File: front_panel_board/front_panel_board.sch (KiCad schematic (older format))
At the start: 9 parts, among them J1 Molex_SL_01x02_Male, J2 Conn_02x05_Odd_Even, J3 Molex_SL_01x02_Male, SW1 SW_Rotary8, SW2 SW_SPST

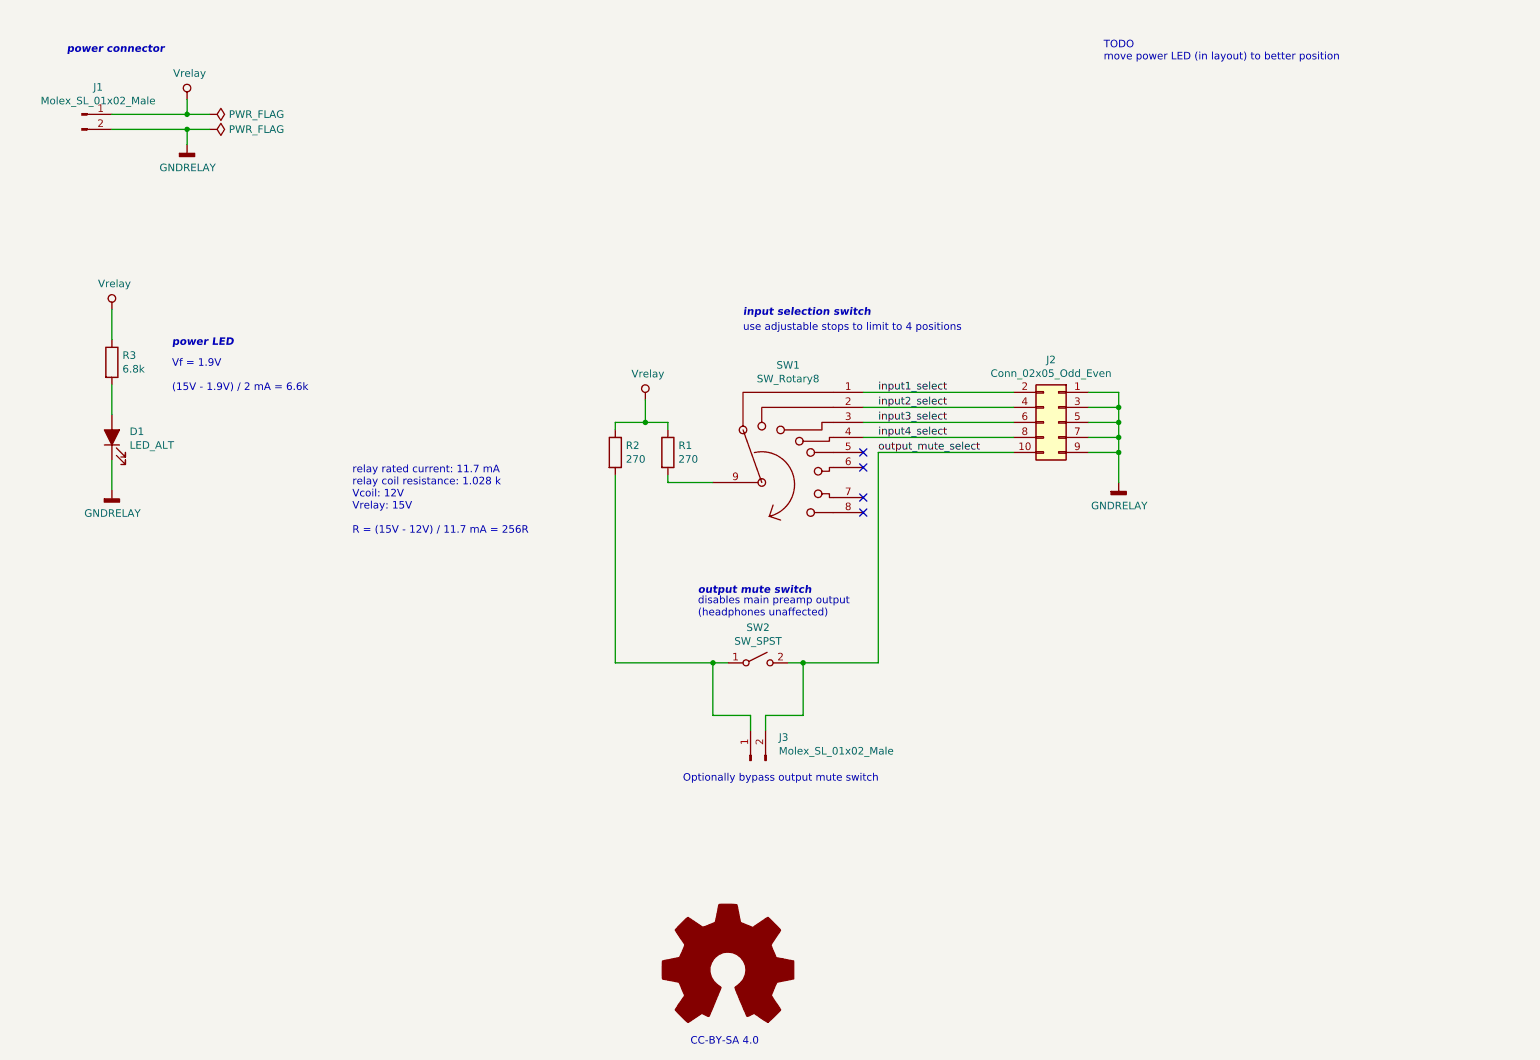
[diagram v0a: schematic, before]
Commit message: update switch symbol/footprint, add second relay control connector, and re-layout (LED not laid out)
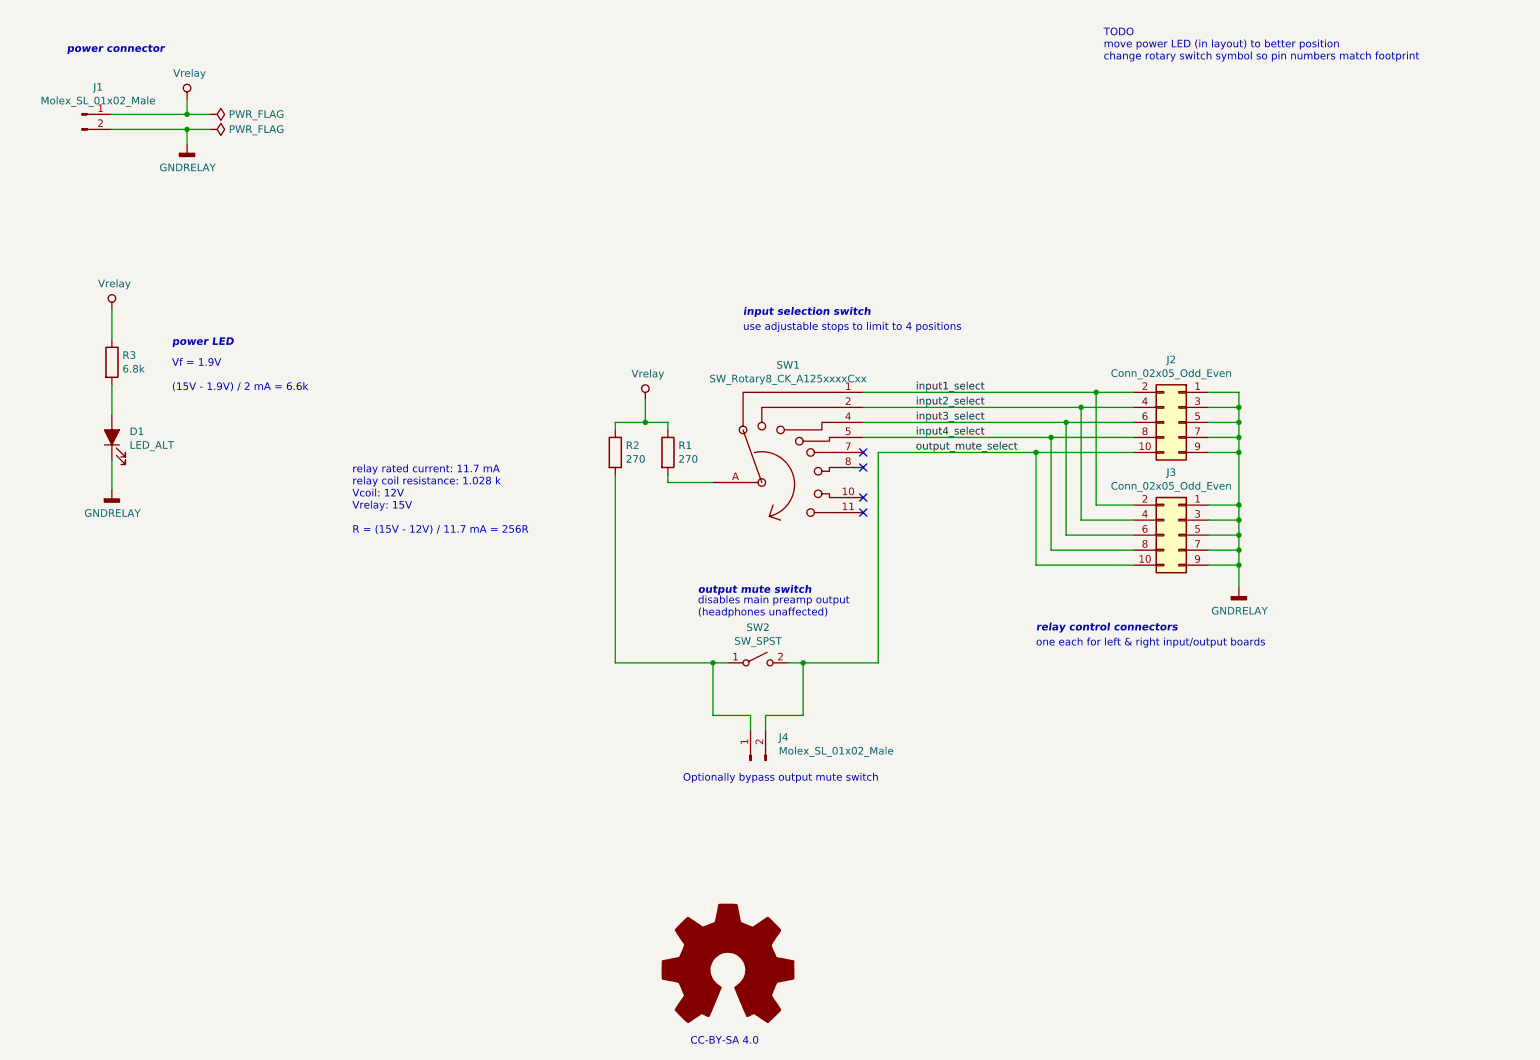
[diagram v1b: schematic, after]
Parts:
- removed SW1: SW_Rotary8, Button_Switch_THT_gkeeth:SW_Rotary8_C&K_A125xxxxCxx, symbol Switch_gkeeth:SW_Rotary8
- added J3: Conn_02x05_Odd_Even, Connector_Molex_C-Grid:Molex_C-Grid_70246-1001_2x05_P2.54mm_Vertical, symbol Connector_Generic:Conn_02x05_Odd_Even
- added SW1: SW_Rotary8_CK_A125xxxxCxx, Button_Switch_THT_gkeeth:SW_Rotary8_CK_A125xxxxCxx, symbol Switch_gkeeth:SW_Rotary8_CK_A125xxxxCxx
- renumbered J3 to J4
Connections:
- net GNDRELAY: now also J3.1 (Pin_1), J3.3 (Pin_3), J3.5 (Pin_5), J3.7 (Pin_7), J3.9 (Pin_9)
- net input1_select: now also J3.2 (Pin_2), SW1.1
- net input2_select: now also J3.4 (Pin_4), SW1.2
- net input3_select: now also J3.6 (Pin_6), SW1.4
- net input4_select: now also J3.8 (Pin_8), SW1.5
- net output_mute_select: now also J3.10 (Pin_10)
- net at R1.2: now also SW1.A
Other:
- note added: "TODO\nmove power LED (in layout) to better position\nchange rotary switch symbol so pin numbers match footprint"
- note added: "one each for left & right input/output boards"
- note added: "relay control connectors"
- note removed: "TODO\nmove power LED (in layout) to better position"
- moved on the sheet: J2
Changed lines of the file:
@@
-$EndComp
-$Comp
-L Connector_Generic:Conn_02x05_Odd_Even J2
-U 1 1 5CD2571D
-P 7700 3500
-F 0 "J2" H 7750 3917 50  0000 C CNN
-F 1 "Conn_02x05_Odd_Even" H 7750 3826 50  0000 C CNN
-F 2 "Connector_Molex_C-Grid:Molex_C-Grid_70246-1001_2x05_P2.54mm_Vertical" H 7700 3500 50  0001 C CNN
-F 3 "~" H 7700 3500 50  0001 C CNN
-	1    7700 3500
-	-1   0    0    -1
 $EndComp
 $Comp
@@
 	1900 1450 1900 1350
 Wire Wire Line
-	6400 3300 7400 3300
-Wire Wire Line
-	7400 3400 6400 3400
-Wire Wire Line
-	6400 3500 7400 3500
-Wire Wire Line
-	7400 3600 6400 3600
-Text Label 6500 3300 0    50   ~ 0
-input1_select
-Text Label 6500 3400 0    50   ~ 0
-input2_select
-Text Label 6500 3500 0    50   ~ 0
-input3_select
-Text Label 6500 3600 0    50   ~ 0
-input4_select
-Wire Wire Line
 	5900 5100 6000 5100
-Wire Wire Line
-	6500 3700 7400 3700
-Text Label 6500 3700 0    50   ~ 0
-output_mute_select
 $Comp
 L power_gkeeth:Vrelay #PWR0103
@@
 Text Notes 5600 2800 0    50   Italic 10
 input selection switch
-$Comp
-L power_gkeeth:GNDRELAY #PWR0105
-U 1 1 5CD37D01
-P 8100 3900
-F 0 "#PWR0105" H 8100 3650 50  0001 C CNN
-F 1 "GNDRELAY" H 8104 3745 50  0000 C CNN
-F 2 "" H 8100 3900 50  0001 C CNN
-F 3 "" H 8100 3900 50  0001 C CNN
-	1    8100 3900
-	1    0    0    -1
-$EndComp
-Wire Wire Line
-	8100 3900 8100 3700
-Wire Wire Line
-	8100 3300 7900 3300
-Wire Wire Line
-	7900 3400 8100 3400
-Connection ~ 8100 3400
-Wire Wire Line
-	8100 3400 8100 3300
-Wire Wire Line
-	7900 3500 8100 3500
-Connection ~ 8100 3500
-Wire Wire Line
-	8100 3500 8100 3400
-Wire Wire Line
-	7900 3600 8100 3600
-Connection ~ 8100 3600
-Wire Wire Line
-	8100 3600 8100 3500
-Wire Wire Line
-	7900 3700 8100 3700
-Connection ~ 8100 3700
-Wire Wire Line
-	8100 3700 8100 3600
 Wire Wire Line
 	1400 3250 1400 3450
@@
 Vf = 1.9V\n\n(15V - 1.9V) / 2 mA = 6.6k
 Text Notes 8000 1100 0    50   ~ 0
-TODO\nmove power LED (in layout) to better position
-$Comp
-L Graphic:Logo_Open_Hardware_Large #LOGO?
+TODO\nmove power LED (in layout) to better position\nchange rotary switch symbol so pin numbers match footprint
+$Comp
+L Graphic:Logo_Open_Hardware_Large #LOGO1
 U 1 1 5D0E05C4
 P 5500 7150
-F 0 "#LOGO?" H 5500 7650 50  0001 C CNN
+F 0 "#LOGO1" H 5500 7650 50  0001 C CNN
 F 1 "Logo_Open_Hardware_Large" H 5500 6750 50  0001 C CNN
 F 2 "" H 5500 7150 50  0001 C CNN
@@
 CC-BY-SA 4.0
 $Comp
-L Switch_gkeeth:SW_Rotary8 SW1
-U 1 1 5D180485
-P 6000 3900
-F 0 "SW1" H 5900 4681 50  0000 C CNN
-F 1 "SW_Rotary8" H 5900 4590 50  0000 C CNN
-F 2 "Button_Switch_THT_gkeeth:SW_Rotary8_C&K_A125xxxxCxx" H 5800 4600 50  0001 C CNN
-F 3 "" H 5800 4600 50  0001 C CNN
-F 4 "C&K" H 6000 3900 50  0001 C CNN "Manufacturer"
-F 5 "A11205RNCQ" H 6000 3900 50  0001 C CNN "Manufacturer PN"
-	1    6000 3900
-	1    0    0    -1
-$EndComp
-$Comp
-L Connector_gkeeth:Molex_SL_01x02_Male J3
+L Connector_gkeeth:Molex_SL_01x02_Male J4
 U 1 1 5D183CB3
 P 5650 5750
-F 0 "J3" V 5804 5562 50  0000 R CNN
+F 0 "J4" V 5804 5562 50  0000 R CNN
 F 1 "Molex_SL_01x02_Male" V 5713 5562 50  0000 R CNN
 F 2 "Connector_Molex_SL:Molex_SL_A-70543-0001_1x02_P2.54mm_Vertical" H 5650 5750 50  0001 C CNN
@@
 	1    0    0    -1
 $EndComp
+Text Label 6750 3700 0    50   ~ 0
+output_mute_select
+Text Label 6750 3600 0    50   ~ 0
+input4_select
+Text Label 6750 3500 0    50   ~ 0
+input3_select
+Text Label 6750 3400 0    50   ~ 0
+input2_select
+Text Label 6750 3300 0    50   ~ 0
+input1_select
+Connection ~ 7550 3700
+Wire Wire Line
+	6500 3700 7550 3700
+Wire Wire Line
+	7550 3700 7550 4450
+Wire Wire Line
+	7650 3600 6400 3600
+Connection ~ 7650 3600
+Wire Wire Line
+	7650 3600 7650 4350
+Connection ~ 7750 3500
+Wire Wire Line
+	6400 3500 7750 3500
+Wire Wire Line
+	7750 3500 7750 4250
+Wire Wire Line
+	7850 3400 6400 3400
+Connection ~ 7850 3400
+Wire Wire Line
+	7850 3400 7850 4150
+Wire Wire Line
+	6400 3300 7950 3300
+Connection ~ 7950 3300
+Wire Wire Line
+	7950 4050 7950 3300
+Wire Wire Line
+	8900 4450 8900 4350
+Connection ~ 8900 4450
+Wire Wire Line
+	8700 4450 8900 4450
+Wire Wire Line
+	8900 4350 8900 4250
+Connection ~ 8900 4350
+Wire Wire Line
+	8700 4350 8900 4350
+Wire Wire Line
+	8900 4250 8900 4150
+Connection ~ 8900 4250
+Wire Wire Line
+	8700 4250 8900 4250
+Wire Wire Line
+	8900 4150 8900 4050
+Connection ~ 8900 4150
+Wire Wire Line
+	8900 4150 8700 4150
+Wire Wire Line
+	8900 4050 8900 3700
+Connection ~ 8900 4050
+Wire Wire Line
+	8700 4050 8900 4050
+Wire Wire Line
+	8900 3700 8900 3600
+Connection ~ 8900 3700
+Wire Wire Line
+	8700 3700 8900 3700
+Wire Wire Line
+	8900 3600 8900 3500
+Connection ~ 8900 3600
+Wire Wire Line
+	8700 3600 8900 3600
+Wire Wire Line
+	8900 3500 8900 3400
+Connection ~ 8900 3500
+Wire Wire Line
+	8700 3500 8900 3500
+Wire Wire Line
+	8900 3400 8900 3300
+Connection ~ 8900 3400
+Wire Wire Line
+	8700 3400 8900 3400
+Wire Wire Line
+	8900 3300 8700 3300
+Wire Wire Line
+	8900 4600 8900 4450
+$Comp
+L power_gkeeth:GNDRELAY #PWR0105
+U 1 1 5CD37D01
+P 8900 4600
+F 0 "#PWR0105" H 8900 4350 50  0001 C CNN
+F 1 "GNDRELAY" H 8904 4445 50  0000 C CNN
+F 2 "" H 8900 4600 50  0001 C CNN
+F 3 "" H 8900 4600 50  0001 C CNN
+	1    8900 4600
+	1    0    0    -1
+$EndComp
+Text Notes 7550 4900 0    50   Italic 10
+relay control connectors
+Text Notes 7550 5000 0    50   ~ 0
+one each for left & right input/output boards
+$Comp
+L Switch_gkeeth:SW_Rotary8_CK_A125xxxxCxx SW1
+U 1 1 5D13D52B
+P 6000 3900
+F 0 "SW1" H 5900 4681 50  0000 C CNN
+F 1 "SW_Rotary8_CK_A125xxxxCxx" H 5900 4590 50  0000 C CNN
+F 2 "Button_Switch_THT_gkeeth:SW_Rotary8_CK_A125xxxxCxx" H 5800 4600 50  0001 C CNN
+F 3 "https://www.ckswitches.com/media/1349/arotary.pdf" H 5800 4600 50  0001 C CNN
+	1    6000 3900
+	1    0    0    -1
+$EndComp
+Wire Wire Line
+	7650 4350 8200 4350
+Wire Wire Line
+	7750 4250 8200 4250
+Wire Wire Line
+	7850 4150 8200 4150
+Wire Wire Line
+	8200 4050 7950 4050
+Wire Wire Line
+	7550 4450 8200 4450
+$Comp
+L Connector_Generic:Conn_02x05_Odd_Even J3
+U 1 1 5D106F42
+P 8500 4250
+F 0 "J3" H 8550 4667 50  0000 C CNN
+F 1 "Conn_02x05_Odd_Even" H 8550 4576 50  0000 C CNN
+F 2 "Connector_Molex_C-Grid:Molex_C-Grid_70246-1001_2x05_P2.54mm_Vertical" H 8500 4250 50  0001 C CNN
+F 3 "~" H 8500 4250 50  0001 C CNN
+	1    8500 4250
+	-1   0    0    -1
+$EndComp
+Wire Wire Line
+	8200 3600 7650 3600
+Wire Wire Line
+	7750 3500 8200 3500
+Wire Wire Line
+	8200 3400 7850 3400
+Wire Wire Line
+	7950 3300 8200 3300
+Wire Wire Line
+	7550 3700 8200 3700
+$Comp
+L Connector_Generic:Conn_02x05_Odd_Even J2
+U 1 1 5CD2571D
+P 8500 3500
+F 0 "J2" H 8550 3917 50  0000 C CNN
+F 1 "Conn_02x05_Odd_Even" H 8550 3826 50  0000 C CNN
+F 2 "Connector_Molex_C-Grid:Molex_C-Grid_70246-1001_2x05_P2.54mm_Vertical" H 8500 3500 50  0001 C CNN
+F 3 "~" H 8500 3500 50  0001 C CNN
+	1    8500 3500
+	-1   0    0    -1
+$EndComp
 $EndSCHEMATC

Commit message: update net labelling, change to SPDT switch for headphone selection, and clean up schematic
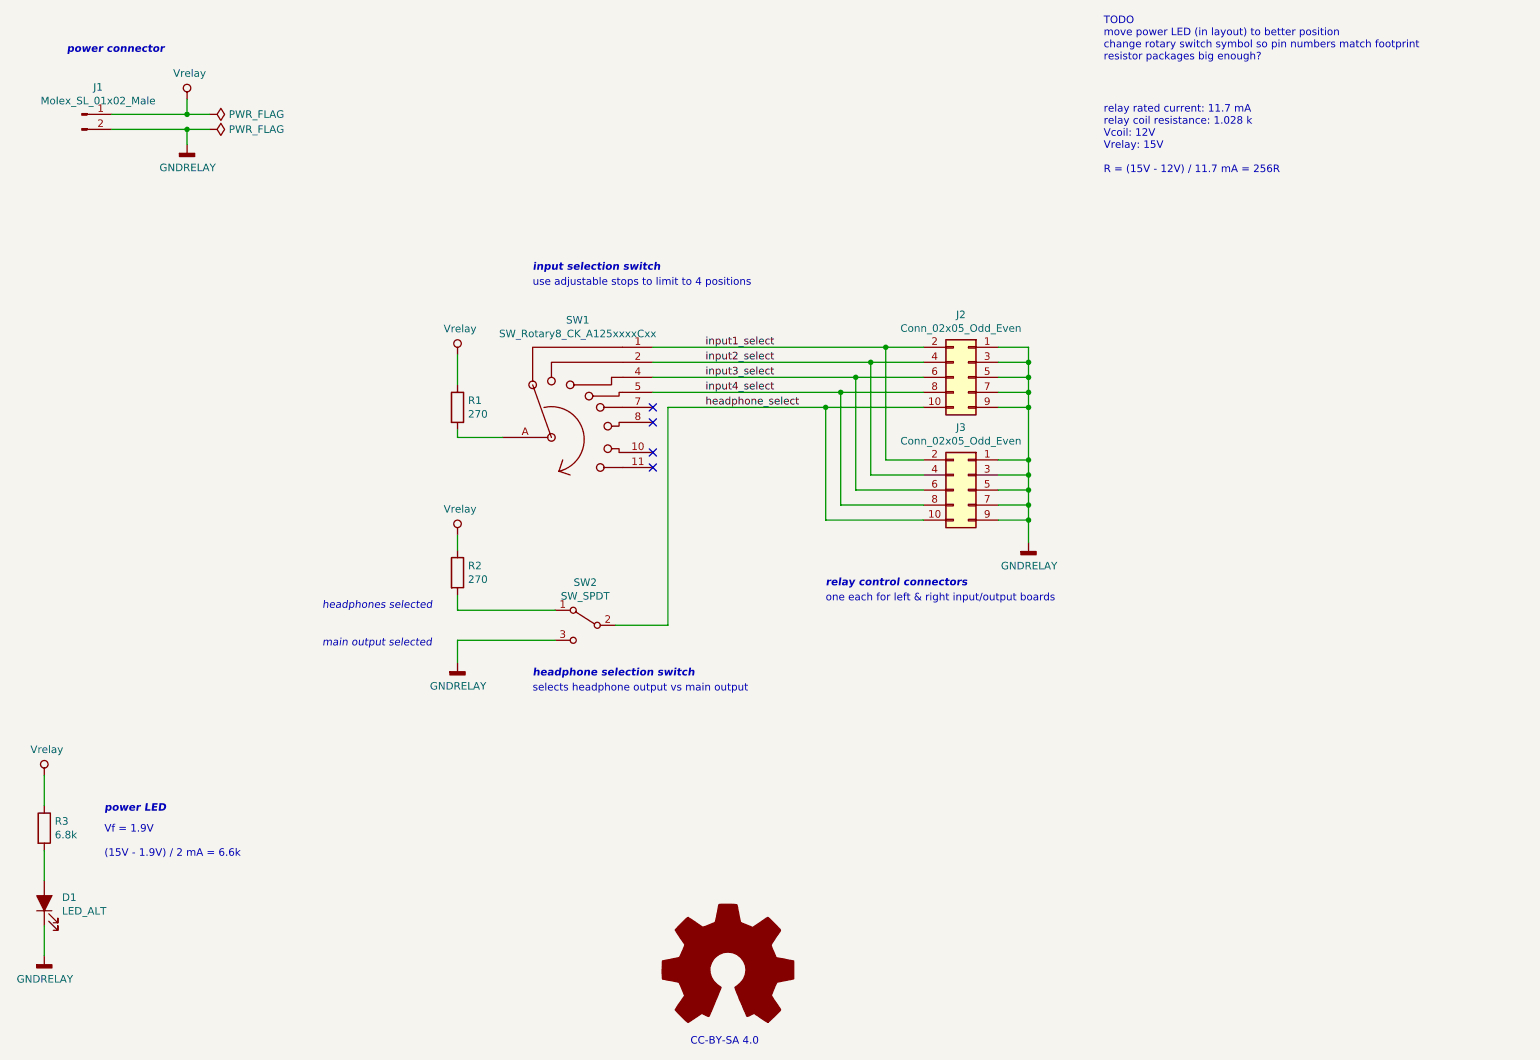
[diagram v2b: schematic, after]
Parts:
- removed J4: Molex_SL_01x02_Male, Connector_Molex_SL:Molex_SL_A-70543-0001_1x02_P2.54mm_Vertical, symbol Connector_gkeeth:Molex_SL_01x02_Male
- removed SW2: SW_SPST, Button_Switch_THT_gkeeth:SW_Toggle_SPST_NKK_M2011xxx03, symbol Switch:SW_SPST
- added SW2: SW_SPDT, Button_Switch_THT_gkeeth:SW_Toggle_SPDT_NKK_M201xxxx03, symbol Switch:SW_SPDT
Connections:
- net GNDRELAY: now also SW2.3 (C)
- net at R2.2: now also SW2.1 (A)
- net output_mute_select renamed headphone_select
- net headphone_select: now also SW2.2 (B)
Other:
- note added: "TODO\nmove power LED (in layout) to better position\nchange rotary switch symbol so pin numbers match footprint\nresistor packages big enough?"
- note added: "headphone selection switch"
- note added: "headphones selected"
- note added: "main output selected"
- note added: "selects headphone output vs main output"
- note removed: "Optionally bypass output mute switch"
- note removed: "TODO\nmove power LED (in layout) to better position\nchange rotary switch symbol so pin numbers match footprint"
- note removed: "disables main preamp output\n(headphones unaffected)"
- note removed: "output mute switch"
- moved on the sheet: D1, J2, J3, R1, R2, R3, SW1
